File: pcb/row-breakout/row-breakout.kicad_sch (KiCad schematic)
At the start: 4 parts, among them J1 AudioJack4_SwitchTR1, J2 Conn_01x02, J3 RJ45, J4 Conn_01x08

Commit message: Create Gerbers
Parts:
- added H1: MountingHole, MountingHole:MountingHole_2.7mm_M2.5, symbol Mechanical:MountingHole
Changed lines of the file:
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@@
     (stroke (width 0) (type default) (color 0 0 0 0))
+  )
+  (symbol (lib_id "Mechanical:MountingHole") (at 74.93 34.925 0) (unit 1)
+    (in_bom yes) (on_board yes) (fields_autoplaced)
+    (property "Reference" "H1" (id 0) (at 77.47 33.6549 0)
+      (effects (font (size 1.27 1.27)) (justify left))
+    )
+    (property "Value" "MountingHole" (id 1) (at 77.47 36.1949 0)
+      (effects (font (size 1.27 1.27)) (justify left))
+    )
+    (property "Footprint" "MountingHole:MountingHole_2.7mm_M2.5" (id 2) (at 74.93 34.925 0)
+      (effects (font (size 1.27 1.27)) hide)
+    )
+    (property "Datasheet" "~" (id 3) (at 74.93 34.925 0)
+      (effects (font (size 1.27 1.27)) hide)
+    )
   )
   (symbol (lib_id "Connector_Generic:Conn_01x02") (at 72.39 45.72 0) (unit 1)
@@
   )
   (symbol_instances
+    (path "/0dfdfa9f-1e3f-4e14-b64b-12bde76a80c7"
+      (reference "H1") (unit 1) (value "MountingHole") (footprint "MountingHole:MountingHole_2.7mm_M2.5")
+    )
     (path "/ae0e6b31-27d7-4383-a4fc-7557b0a19382"
       (reference "J1") (unit 1) (value "AudioJack4_SwitchTR1") (footprint "AudioJack:AudioJack4_6pad")

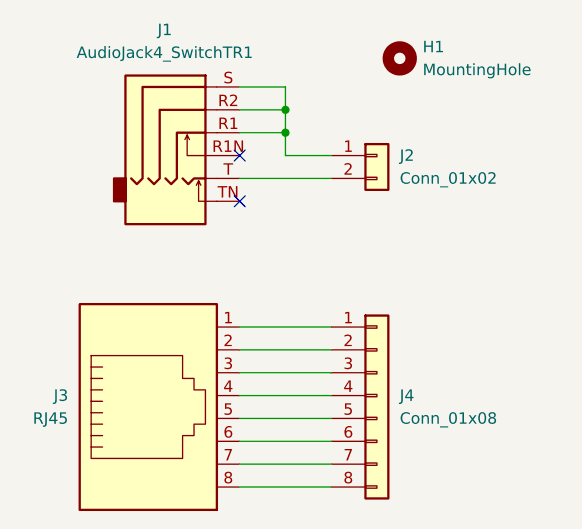
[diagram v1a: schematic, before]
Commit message: Add Grounded Copper Fills to Row Breakout and Main Board
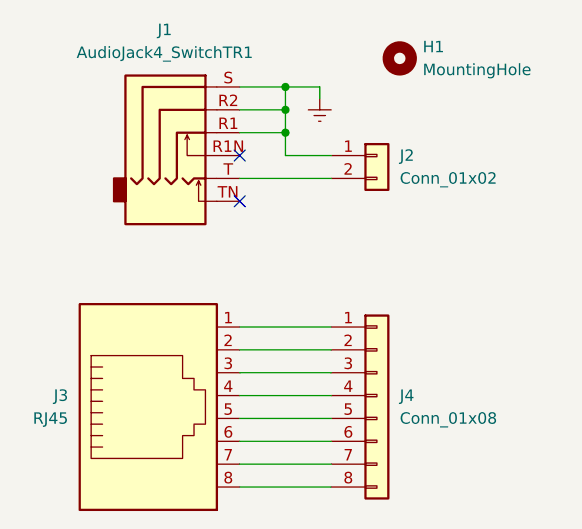
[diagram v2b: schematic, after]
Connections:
- net Earth: now reaches J1.R1, J1.R2, J1.S, J2.1 (Pin_1)
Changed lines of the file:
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@@
   (junction (at 62.23 43.18) (diameter 0) (color 0 0 0 0)
+  )
+  (junction (at 62.23 38.1) (diameter 0) (color 0 0 0 0)
   )
   (junction (at 62.23 40.64) (diameter 0) (color 0 0 0 0)
@@
   (no_connect (at 57.15 50.8))
   (wire (pts (xy 57.15 38.1) (xy 62.23 38.1))
+    (stroke (width 0) (type default) (color 0 0 0 0))
+  )
+  (wire (pts (xy 66.04 39.37) (xy 66.04 38.1))
     (stroke (width 0) (type default) (color 0 0 0 0))
   )
@@
     (stroke (width 0) (type default) (color 0 0 0 0))
   )
+  (wire (pts (xy 66.04 38.1) (xy 62.23 38.1))
+    (stroke (width 0) (type default) (color 0 0 0 0))
+  )
   (symbol (lib_id "Mechanical:MountingHole") (at 74.93 34.925 0) (unit 1)
     (in_bom yes) (on_board yes) (fields_autoplaced)
@@
       (effects (font (size 1.27 1.27)) hide)
     )
+  )
+  (symbol (lib_id "power:Earth") (at 66.04 39.37 0) (unit 1)
+    (in_bom yes) (on_board yes) (fields_autoplaced)
+    (property "Reference" "#PWR0101" (id 0) (at 66.04 45.72 0)
+      (effects (font (size 1.27 1.27)) hide)
+    )
+    (property "Value" "Earth" (id 1) (at 66.04 43.18 0)
+      (effects (font (size 1.27 1.27)) hide)
+    )
+    (property "Footprint" "" (id 2) (at 66.04 39.37 0)
+      (effects (font (size 1.27 1.27)) hide)
+    )
+    (property "Datasheet" "~" (id 3) (at 66.04 39.37 0)
+      (effects (font (size 1.27 1.27)) hide)
+    )
+    (pin "1")
   )
   (symbol (lib_id "Connector_Generic:Conn_01x02") (at 72.39 45.72 0) (unit 1)
@@
   )
   (symbol_instances
+    (path "/1f9ae101-c652-4998-a503-17aedf3d5746"
+      (reference "#PWR0101") (unit 1) (value "Earth") (footprint "")
+    )
     (path "/0dfdfa9f-1e3f-4e14-b64b-12bde76a80c7"
       (reference "H1") (unit 1) (value "MountingHole") (footprint "MountingHole:MountingHole_2.7mm_M2.5")
